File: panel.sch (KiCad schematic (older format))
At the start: 1 part, among them U1 led-panel-16x16

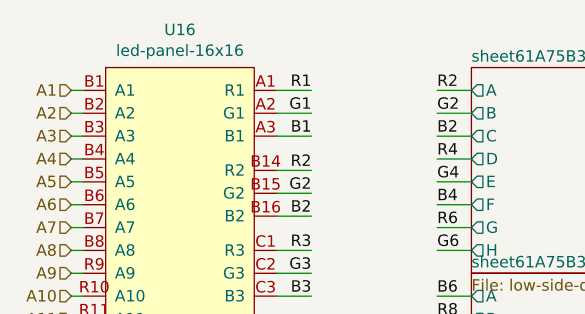
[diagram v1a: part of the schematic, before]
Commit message: Add mounting pad for safety pin
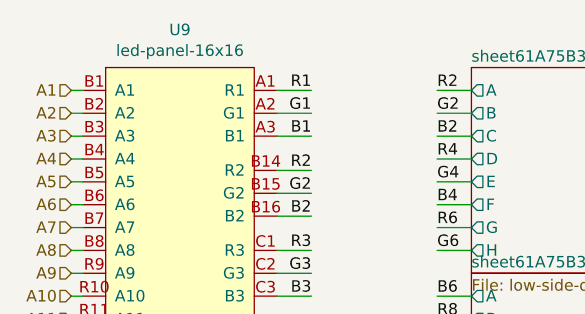
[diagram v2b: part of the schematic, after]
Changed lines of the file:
@@
 $Descr A4 11693 8268
 encoding utf-8
-Sheet 17 25
+Sheet 10 25
 Title ""
 Date ""
@@
 AR Path="/61C4C20D/61A429F9" Ref="U9"  Part="1"
 AR Path="/61C4C905/61A429F9" Ref="U16"  Part="1"
-F 0 "U16" H 3625 6915 50  0000 C CNN
+F 0 "U9" H 3625 6915 50  0000 C CNN
 F 1 "led-panel-16x16" H 3625 6824 50  0000 C CNN
 F 2 "led-panel:bga-led-panel-16x16" H 3400 6800 50  0001 C CNN

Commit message: Add missing part references
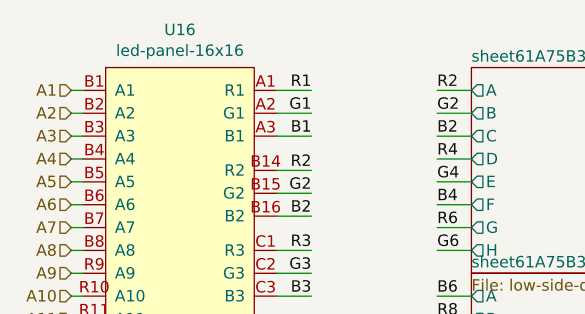
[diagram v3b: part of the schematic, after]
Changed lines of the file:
@@
 $Descr A4 11693 8268
 encoding utf-8
-Sheet 10 25
+Sheet 17 25
 Title ""
 Date ""
@@
 AR Path="/61C4C20D/61A429F9" Ref="U9"  Part="1"
 AR Path="/61C4C905/61A429F9" Ref="U16"  Part="1"
-F 0 "U9" H 3625 6915 50  0000 C CNN
+F 0 "U16" H 3625 6915 50  0000 C CNN
 F 1 "led-panel-16x16" H 3625 6824 50  0000 C CNN
 F 2 "led-panel:bga-led-panel-16x16" H 3400 6800 50  0001 C CNN
